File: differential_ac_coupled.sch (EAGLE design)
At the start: 25 parts, among them U1 AD8421

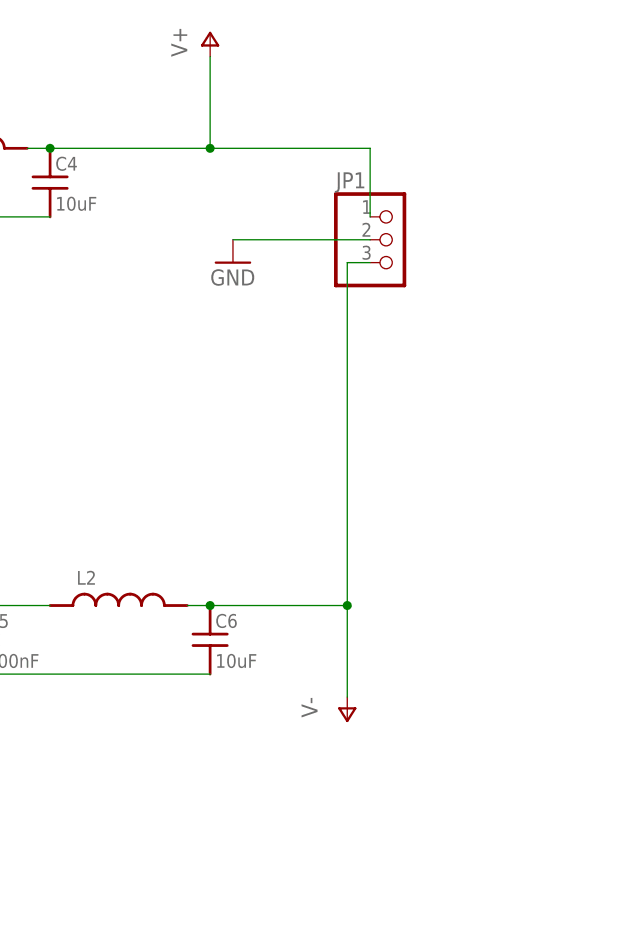
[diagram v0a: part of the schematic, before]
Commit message: Add battery holders
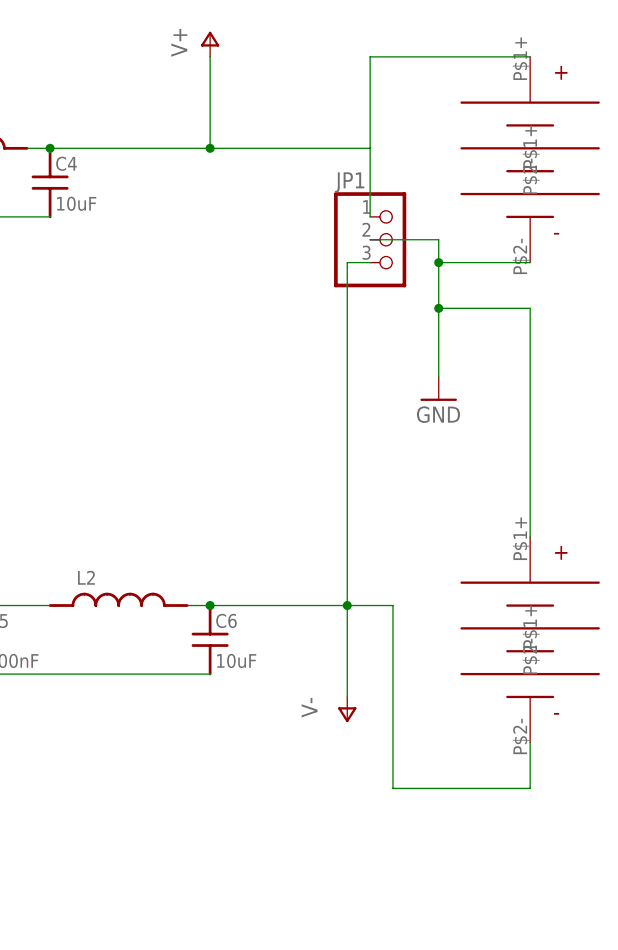
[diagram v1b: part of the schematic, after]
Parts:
- added U$1, U$2: BATT-HOLDER, regulator-jqi:BATT-HOLDER
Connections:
- net GND: now also U$1.P$2-, U$2.P$1+
- net V+: now also U$1.P$1+
- net V-: now also U$2.P$2-
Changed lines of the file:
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@@
 <?xml version="1.0" encoding="utf-8"?>
 <!DOCTYPE eagle SYSTEM "eagle.dtd">
-<eagle version="6.6.0">
+<eagle version="6.5.0">
 <drawing>
 <settings>
@@
 <part name="R8" library="jqi_passives" deviceset="R_SMD" device="R1206"/>
 <part name="R9" library="jqi_passives" deviceset="R_SMD" device="R1206" value="0R"/>
+<part name="U$1" library="regulator-jqi" deviceset="BATT-HOLDER" device=""/>
+<part name="U$2" library="regulator-jqi" deviceset="BATT-HOLDER" device=""/>
 </parts>
 <sheets>
@@
 <instance part="P-1" gate="1" x="144.78" y="40.64"/>
 <instance part="JP1" gate="A" x="149.86" y="93.98"/>
-<instance part="GND6" gate="1" x="132.08" y="91.44"/>
+<instance part="GND6" gate="1" x="154.94" y="76.2"/>
 <instance part="IN-" gate="G$1" x="-38.1" y="76.2"/>
 <instance part="IN+" gate="G$1" x="-25.4" y="48.26"/>
@@
 <instance part="R8" gate="G$1" x="-17.78" y="38.1" rot="R90"/>
 <instance part="R9" gate="G$1" x="-27.94" y="76.2" rot="R180"/>
+<instance part="U$1" gate="G$1" x="165.1" y="101.6"/>
+<instance part="U$2" gate="G$1" x="165.1" y="48.26"/>
 </instances>
 <busses>
@@
 <pinref part="JP1" gate="A" pin="2"/>
 <pinref part="GND6" gate="1" pin="GND"/>
-<wire x1="147.32" y1="93.98" x2="132.08" y2="93.98" width="0.1524" layer="91"/>
+<wire x1="147.32" y1="93.98" x2="154.94" y2="93.98" width="0.1524" layer="91"/>
+<wire x1="154.94" y1="93.98" x2="154.94" y2="91.44" width="0.1524" layer="91"/>
+<pinref part="U$1" gate="G$1" pin="P$2-"/>
+<wire x1="154.94" y1="91.44" x2="154.94" y2="86.36" width="0.1524" layer="91"/>
+<wire x1="154.94" y1="86.36" x2="154.94" y2="78.74" width="0.1524" layer="91"/>
+<wire x1="165.1" y1="91.44" x2="154.94" y2="91.44" width="0.1524" layer="91"/>
+<pinref part="U$2" gate="G$1" pin="P$1+"/>
+<wire x1="165.1" y1="60.96" x2="165.1" y2="86.36" width="0.1524" layer="91"/>
+<wire x1="165.1" y1="86.36" x2="154.94" y2="86.36" width="0.1524" layer="91"/>
+<junction x="154.94" y="91.44"/>
+<junction x="154.94" y="86.36"/>
 </segment>
 <segment>
@@
 <wire x1="144.78" y1="91.44" x2="144.78" y2="53.34" width="0.1524" layer="91"/>
 <junction x="144.78" y="53.34"/>
+<pinref part="U$2" gate="G$1" pin="P$2-"/>
+<wire x1="165.1" y1="38.1" x2="165.1" y2="33.02" width="0.1524" layer="91"/>
+<wire x1="165.1" y1="33.02" x2="149.86" y2="33.02" width="0.1524" layer="91"/>
+<wire x1="149.86" y1="33.02" x2="149.86" y2="53.34" width="0.1524" layer="91"/>
+<wire x1="149.86" y1="53.34" x2="144.78" y2="53.34" width="0.1524" layer="91"/>
 </segment>
 </net>
@@
 <wire x1="147.32" y1="104.14" x2="147.32" y2="96.52" width="0.1524" layer="91"/>
 <junction x="129.54" y="104.14"/>
-</segment>
-</net>
+<pinref part="U$1" gate="G$1" pin="P$1+"/>
+<wire x1="165.1" y1="114.3" x2="147.32" y2="114.3" width="0.1524" layer="91"/>
+<wire x1="147.32" y1="114.3" x2="147.32" y2="104.14" width="0.1524" layer="91"/>
+</segment>
+</net>
